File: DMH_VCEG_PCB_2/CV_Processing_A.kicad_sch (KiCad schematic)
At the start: 58 parts, among them J22 Conn_01x10_PinHeader, Q11 BC558, Q12 BC558, Q13 BC548, Q14 BC548, Q15 BC548, Q16 BC548, U10 TL074, U8 TL074, U9 TL074

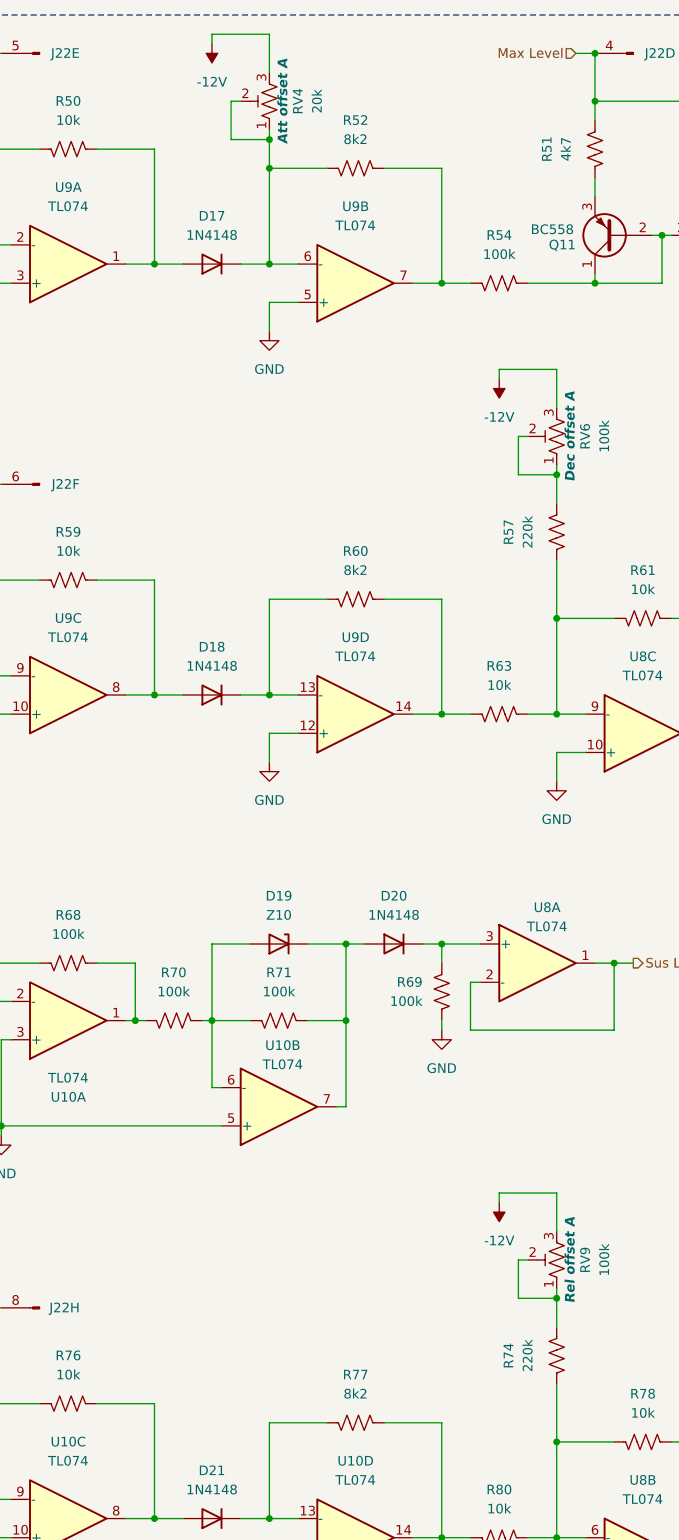
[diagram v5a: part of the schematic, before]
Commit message: Synced PCB 1 and 2
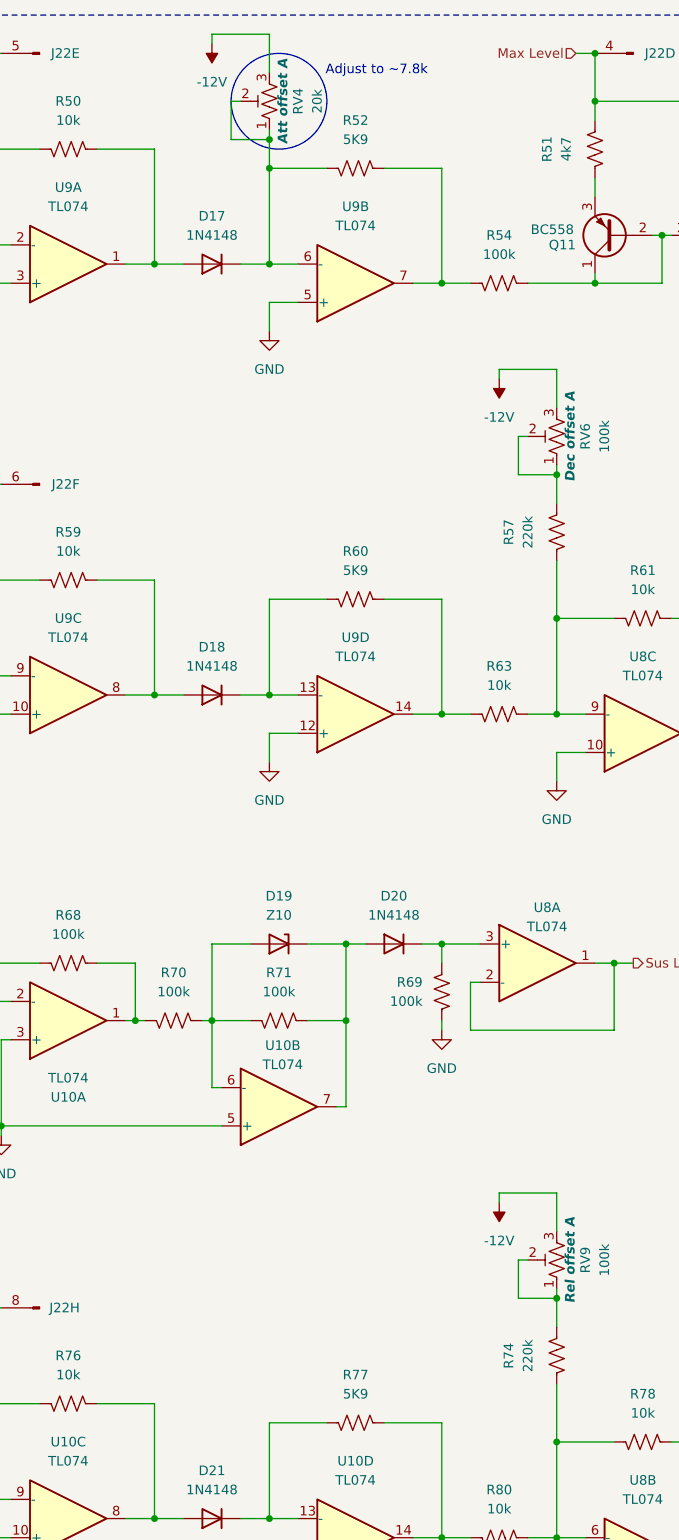
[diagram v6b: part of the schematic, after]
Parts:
- R52, R60, R77: value 8k2 -> 5K9
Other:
- note added: "Adjust to ~7.8k"
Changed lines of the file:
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@@
 		)
 	)
+	(circle
+		(center 85.09 25.4)
+		(radius 6.35)
+		(stroke
+			(width 0)
+			(type default)
+		)
+		(fill
+			(type none)
+		)
+	)
+	(text "Adjust to ~7.8k"
+		(exclude_from_sim no)
+		(at 98.044 21.336 0)
+		(effects
+			(font
+				(size 1.27 1.27)
+			)
+		)
+	)
 	(text "PCB 2"
 		(exclude_from_sim no)
@@
 			)
 		)
-		(property "Value" "8k2"
+		(property "Value" "5K9"
 			(at 95.25 30.48 90)
 			(effects
@@
 			)
 		)
-		(property "Value" "8k2"
+		(property "Value" "5K9"
 			(at 95.25 196.85 90)
 			(effects
@@
 			)
 		)
-		(property "Value" "8k2"
+		(property "Value" "5K9"
 			(at 95.25 87.63 90)
 			(effects

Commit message: Restarted component placing on Main
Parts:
- renumbered J22 to J21
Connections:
- net Att CV: now also J21.3 (Pin_3); no longer J21.5 (Pin_5)
- net Dec CV: now also J22.7 (Pin_7); no longer J22.6 (Pin_6)
- net Max Level: now also J21.7 (Pin_7); no longer J21.4 (Pin_4)
- net Sus CV: now also J21.2 (Pin_2); no longer J21.7 (Pin_7)
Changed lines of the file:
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@@
 		)
 	)
+	(netclass_flag ""
+		(length 2.54)
+		(shape round)
+		(at 45.72 76.2 0)
+		(fields_autoplaced yes)
+		(effects
+			(font
+				(size 1.27 1.27)
+			)
+			(justify left bottom)
+		)
+		(property "Netclass" "CrossPCB"
+			(at 46.4185 73.66 0)
+			(effects
+				(font
+					(size 1.27 1.27)
+				)
+				(justify left)
+				(hide yes)
+			)
+		)
+		(property "Component Class" ""
+			(at -54.61 66.04 0)
+			(effects
+				(font
+					(size 1.27 1.27)
+					(italic yes)
+				)
+			)
+		)
+	)
+	(netclass_flag ""
+		(length 2.54)
+		(shape round)
+		(at 45.72 185.42 0)
+		(fields_autoplaced yes)
+		(effects
+			(font
+				(size 1.27 1.27)
+			)
+			(justify left bottom)
+		)
+		(property "Netclass" "CrossPCB"
+			(at 46.4185 182.88 0)
+			(effects
+				(font
+					(size 1.27 1.27)
+				)
+				(justify left)
+				(hide yes)
+			)
+		)
+		(property "Component Class" ""
+			(at -54.61 175.26 0)
+			(effects
+				(font
+					(size 1.27 1.27)
+					(italic yes)
+				)
+			)
+		)
+	)
+	(netclass_flag ""
+		(length 2.54)
+		(shape round)
+		(at 33.02 139.7 180)
+		(fields_autoplaced yes)
+		(effects
+			(font
+				(size 1.27 1.27)
+			)
+			(justify right bottom)
+		)
+		(property "Netclass" "CrossPCB"
+			(at 33.7185 142.24 0)
+			(effects
+				(font
+					(size 1.27 1.27)
+				)
+				(justify left)
+				(hide yes)
+			)
+		)
+		(property "Component Class" ""
+			(at -67.31 129.54 0)
+			(effects
+				(font
+					(size 1.27 1.27)
+					(italic yes)
+				)
+			)
+		)
+	)
+	(netclass_flag ""
+		(length 2.54)
+		(shape round)
+		(at 45.72 19.05 0)
+		(fields_autoplaced yes)
+		(effects
+			(font
+				(size 1.27 1.27)
+			)
+			(justify left bottom)
+		)
+		(property "Netclass" "CrossPCB"
+			(at 46.4185 16.51 0)
+			(effects
+				(font
+					(size 1.27 1.27)
+				)
+				(justify left)
+				(hide yes)
+			)
+		)
+		(property "Component Class" ""
+			(at -54.61 8.89 0)
+			(effects
+				(font
+					(size 1.27 1.27)
+					(italic yes)
+				)
+			)
+		)
+	)
+	(netclass_flag ""
+		(length 2.54)
+		(shape round)
+		(at 127 19.05 0)
+		(fields_autoplaced yes)
+		(effects
+			(font
+				(size 1.27 1.27)
+			)
+			(justify left bottom)
+		)
+		(property "Netclass" "CrossPCB"
+			(at 127.6985 16.51 0)
+			(effects
+				(font
+					(size 1.27 1.27)
+				)
+				(justify left)
+				(hide yes)
+			)
+		)
+		(property "Component Class" ""
+			(at 26.67 8.89 0)
+			(effects
+				(font
+					(size 1.27 1.27)
+					(italic yes)
+				)
+			)
+		)
+	)
 	(symbol
 		(lib_id "power:-12V")
@@
 		(lib_id "SynthStuff:Conn_01x10_PinHeader")
 		(at 132.08 19.05 180)
-		(unit 4)
+		(unit 7)
 		(exclude_from_sim no)
 		(in_bom yes)
 		(on_board yes)
 		(dnp no)
-		(property "Reference" "J22"
+		(property "Reference" "J21"
 			(at 137.668 19.05 0)
 			(effects
@@
 			(project "DMH_VCEG_PCB_1"
 				(path "/58f4306d-5387-4983-bb08-41a2313fd315/7d3cb848-7f4a-41b7-b3df-5bb0c19476ef"
-					(reference "J22")
-					(unit 4)
+					(reference "J21")
+					(unit 7)
 				)
 			)
@@
 		(lib_id "SynthStuff:Conn_01x10_PinHeader")
 		(at 53.34 19.05 180)
-		(unit 5)
+		(unit 3)
 		(exclude_from_sim no)
 		(in_bom yes)
 		(on_board yes)
 		(dnp no)
-		(property "Reference" "J22"
+		(property "Reference" "J21"
 			(at 58.674 19.05 0)
 			(effects
@@
 			(project "DMH_VCEG_PCB_2"
 				(path "/58f4306d-5387-4983-bb08-41a2313fd315/7d3cb848-7f4a-41b7-b3df-5bb0c19476ef"
-					(reference "J22")
-					(unit 5)
+					(reference "J21")
+					(unit 3)
 				)
 			)
@@
 		(lib_id "SynthStuff:Conn_01x10_PinHeader")
 		(at 53.34 76.2 180)
-		(unit 6)
+		(unit 7)
 		(exclude_from_sim no)
 		(in_bom yes)
@@
 				(path "/58f4306d-5387-4983-bb08-41a2313fd315/7d3cb848-7f4a-41b7-b3df-5bb0c19476ef"
 					(reference "J22")
-					(unit 6)
+					(unit 7)
 				)
 			)
@@
 		(lib_id "SynthStuff:Conn_01x10_PinHeader")
 		(at 33.02 132.08 270)
-		(unit 7)
+		(unit 2)
 		(exclude_from_sim no)
 		(in_bom yes)
 		(on_board yes)
 		(dnp no)
-		(property "Reference" "J22"
+		(property "Reference" "J21"
 			(at 29.972 130.556 90)
 			(effects
@@
 			(project "DMH_VCEG_PCB_2"
 				(path "/58f4306d-5387-4983-bb08-41a2313fd315/7d3cb848-7f4a-41b7-b3df-5bb0c19476ef"
-					(reference "J22")
-					(unit 7)
+					(reference "J21")
+					(unit 2)
 				)
 			)
